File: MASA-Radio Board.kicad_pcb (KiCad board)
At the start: 4 copper layers, 75.8 x 76.2 mm, 70 parts, among them IC1 FAN4010IL6X_F113, IC2 FAN4010IL6X_F113, J1 Conn_01x02, J2 Conn_01x02_Male, J3 Conn_01x06, J4 Conn_01x03_Male, J5 SC_19-20, J6 Conn_01x06, J7 Conn_01x02, J8 UJ2-MBH-1-SMT-TR, U1 MP5077GG-Z, U2 BL654PA, U3 MIC5504-3.3YM5, U5 MP5077GG-Z, U6 SN74LVC1T45DBVR, U7 SN65HVD1050D, U8 MCP2515-xSO, U9 SN74LVC1T45DBVR

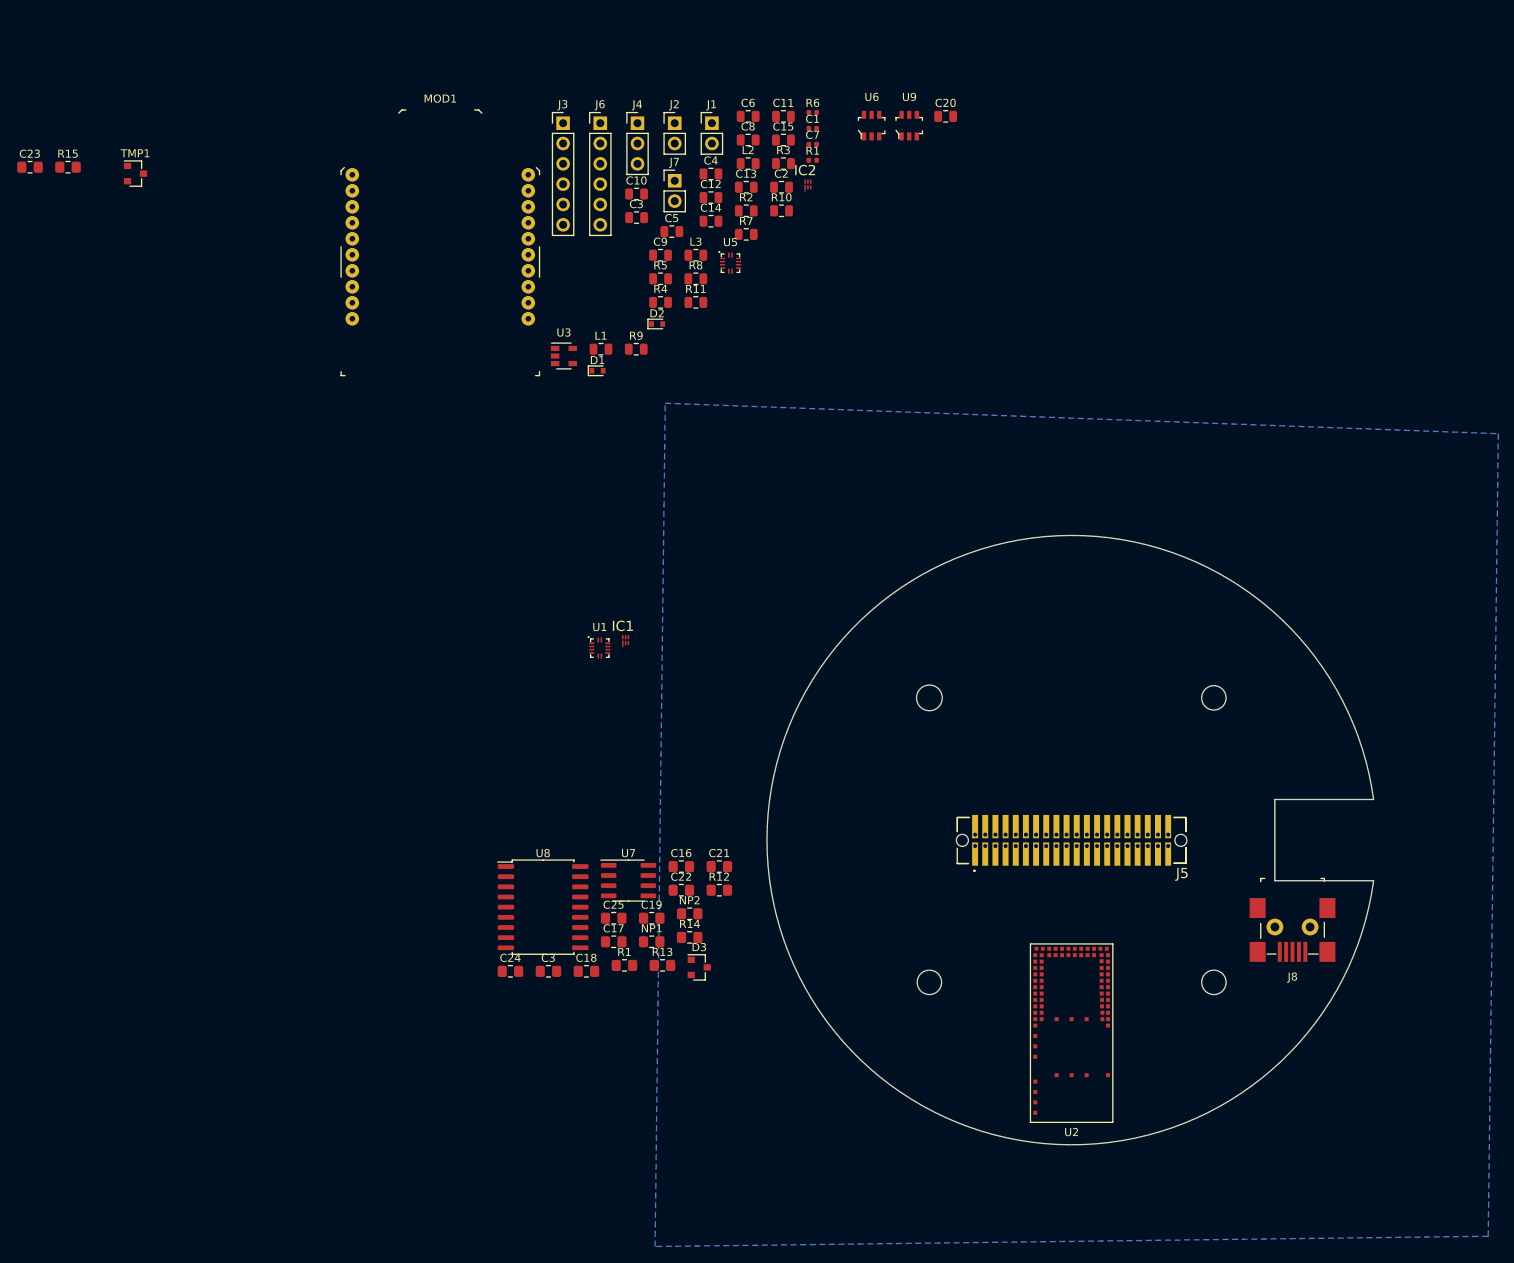
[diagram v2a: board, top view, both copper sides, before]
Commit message: added solder bridges, placed a few components on board
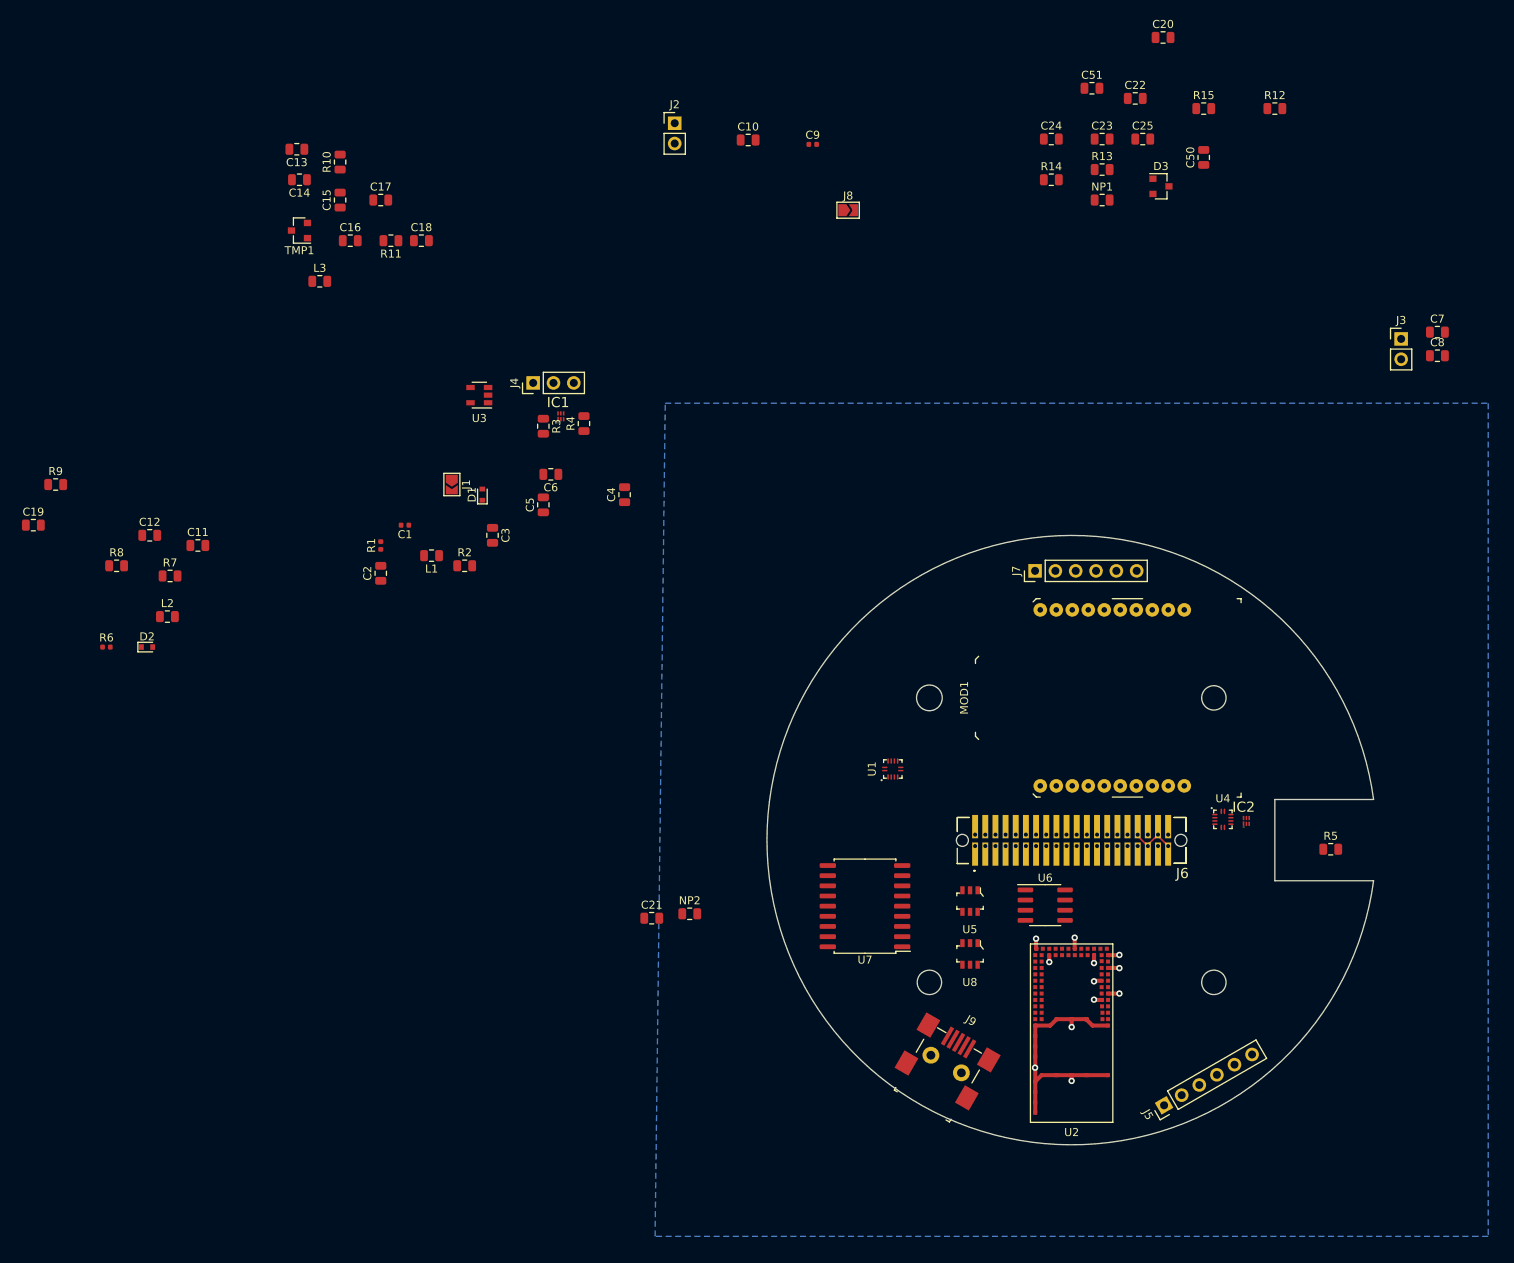
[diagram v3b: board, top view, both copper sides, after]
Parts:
- removed the C3 at (87.0, 143.4)
- removed the R1 at (96.5, 142.7)
- added C7: 47pF, Capacitor_SMD:C_0805_2012Metric, F.Cu at (198.1, 63.5)
- added C8: 1uF, Capacitor_SMD:C_0805_2012Metric, F.Cu at (198.1, 66.5)
- added J3: Conn_01x02_Male, Connector_PinHeader_2.54mm:PinHeader_1x02_P2.54mm_Vertical, F.Cu at (193.6, 64.3)
- C18: renamed from C16; footprint Capacitor_SMD:C_0805_2012Metric_Pad1.15x1.40mm_HandSolder -> Capacitor_SMD:C_0805_2012Metric
- C19: renamed from C17; footprint Capacitor_SMD:C_0805_2012Metric_Pad1.15x1.40mm_HandSolder -> Capacitor_SMD:C_0805_2012Metric
- C20: renamed from C18; footprint Capacitor_SMD:C_0805_2012Metric_Pad1.15x1.40mm_HandSolder -> Capacitor_SMD:C_0805_2012Metric
- C21: renamed from C19; footprint Capacitor_SMD:C_0805_2012Metric_Pad1.15x1.40mm_HandSolder -> Capacitor_SMD:C_0805_2012Metric
- C23: renamed from C21; footprint Capacitor_SMD:C_0805_2012Metric_Pad1.15x1.40mm_HandSolder -> Capacitor_SMD:C_0805_2012Metric
- C24: renamed from C22; footprint Capacitor_SMD:C_0805_2012Metric_Pad1.15x1.40mm_HandSolder -> Capacitor_SMD:C_0805_2012Metric
- C25: renamed from C23; footprint Capacitor_SMD:C_0805_2012Metric_Pad1.15x1.40mm_HandSolder -> Capacitor_SMD:C_0805_2012Metric
- C50: renamed from C24; footprint Capacitor_SMD:C_0805_2012Metric_Pad1.15x1.40mm_HandSolder -> Capacitor_SMD:C_0805_2012Metric
- C51: renamed from C25; footprint Capacitor_SMD:C_0805_2012Metric_Pad1.15x1.40mm_HandSolder -> Capacitor_SMD:C_0805_2012Metric
- J1: footprint Connector_PinHeader_2.54mm:PinHeader_1x02_P2.54mm_Vertical -> Jumper:SolderJumper-2_P1.3mm_Open_TrianglePad1.0x1.5mm
- J8: renamed from J7; footprint Connector_PinHeader_2.54mm:PinHeader_1x02_P2.54mm_Vertical -> Jumper:SolderJumper-2_P1.3mm_Open_TrianglePad1.0x1.5mm
- NP1, NP2, R12, R13, R14, R15: footprint Resistor_SMD:R_0805_2012Metric_Pad1.15x1.40mm_HandSolder -> Resistor_SMD:R_0805_2012Metric
- moved J5 143.9 mm to (164.0, 160.1), turned to 120 degrees
- moved R15 142.2 mm to (168.9, 35.6)
- moved C25 139.1 mm to (161.3, 39.4)
- moved C20 137.2 mm to (163.8, 26.7)
- moved C50 133.6 mm to (168.9, 41.7), turned to 90 degrees
- moved R12 119.9 mm to (177.8, 35.6)
- moved C51 119.7 mm to (154.9, 33.0)
- moved R13 113.7 mm to (156.2, 43.2)
- moved D3 113.4 mm to (163.6, 45.3)
- moved R6 110.7 mm to (31.8, 102.9)
- moved R5 110.0 mm to (184.8, 128.1)
- moved NP1 108.5 mm to (156.2, 47.0)
- moved R14 104.9 mm to (149.9, 44.5)
- moved C24 104.7 mm to (149.9, 39.4)
- moved U8 103.8 mm to (139.7, 141.2), turned to 180 degrees
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- renumbered C8 to C10, C9 to C11, C10 to C12, C11 to C13, C12 to C14, C13 to C15, C14 to C16, C15 to C17, C20 to C22, C5 to C4, C6 to C5, C4 to C6, C7 to C9, J3 to J5, J5 to J6, J6 to J7, J8 to J9, U5 to U4, U6 to U5, U7 to U6, U8 to U7, U9 to U8
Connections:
- J5 pad 2: UART_CTS -> UART_RTS
- J5 pad 6: UART_RTS -> UART_CTS
- U2 pad 1: Net-(U2-Pad1) -> SWDIO
- U2 pad 3: Net-(U2-Pad3) -> SWDCLK
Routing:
- net GND: track 0.00 -> 42.8 mm, vias 0 -> 12
- net 5V0: track 0.00 -> 5.87 mm
- added copper zone on In1.Cu, net +3V3
- added copper zone on B.Cu, net GND
- removed copper zone on B.Cu, net +3V3
- removed copper zone on In1.Cu, net GND
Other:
- rule trace_min: 0.2 -> 0.1524
- rule via_min_drill: 0.3 -> 0.254
- rule via_min_size: 0.4 -> 0.3048

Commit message: Moved components
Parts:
- removed J5: Conn_01x06, Connector_PinHeader_2.54mm:PinHeader_1x06_P2.54mm_Vertical
- moved J7 67.2 mm to (171.9, 156.1), turned to 135 degrees
- moved J9 60.4 mm to (180.6, 120.2), turned to 0 degrees
- moved U2 49.7 mm to (153.1, 101.5), turned to 0 degrees
- moved MOD1 41.6 mm to (151.8, 150.4)
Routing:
- net GND: track 42.8 -> 0.00 mm, vias 12 -> 0

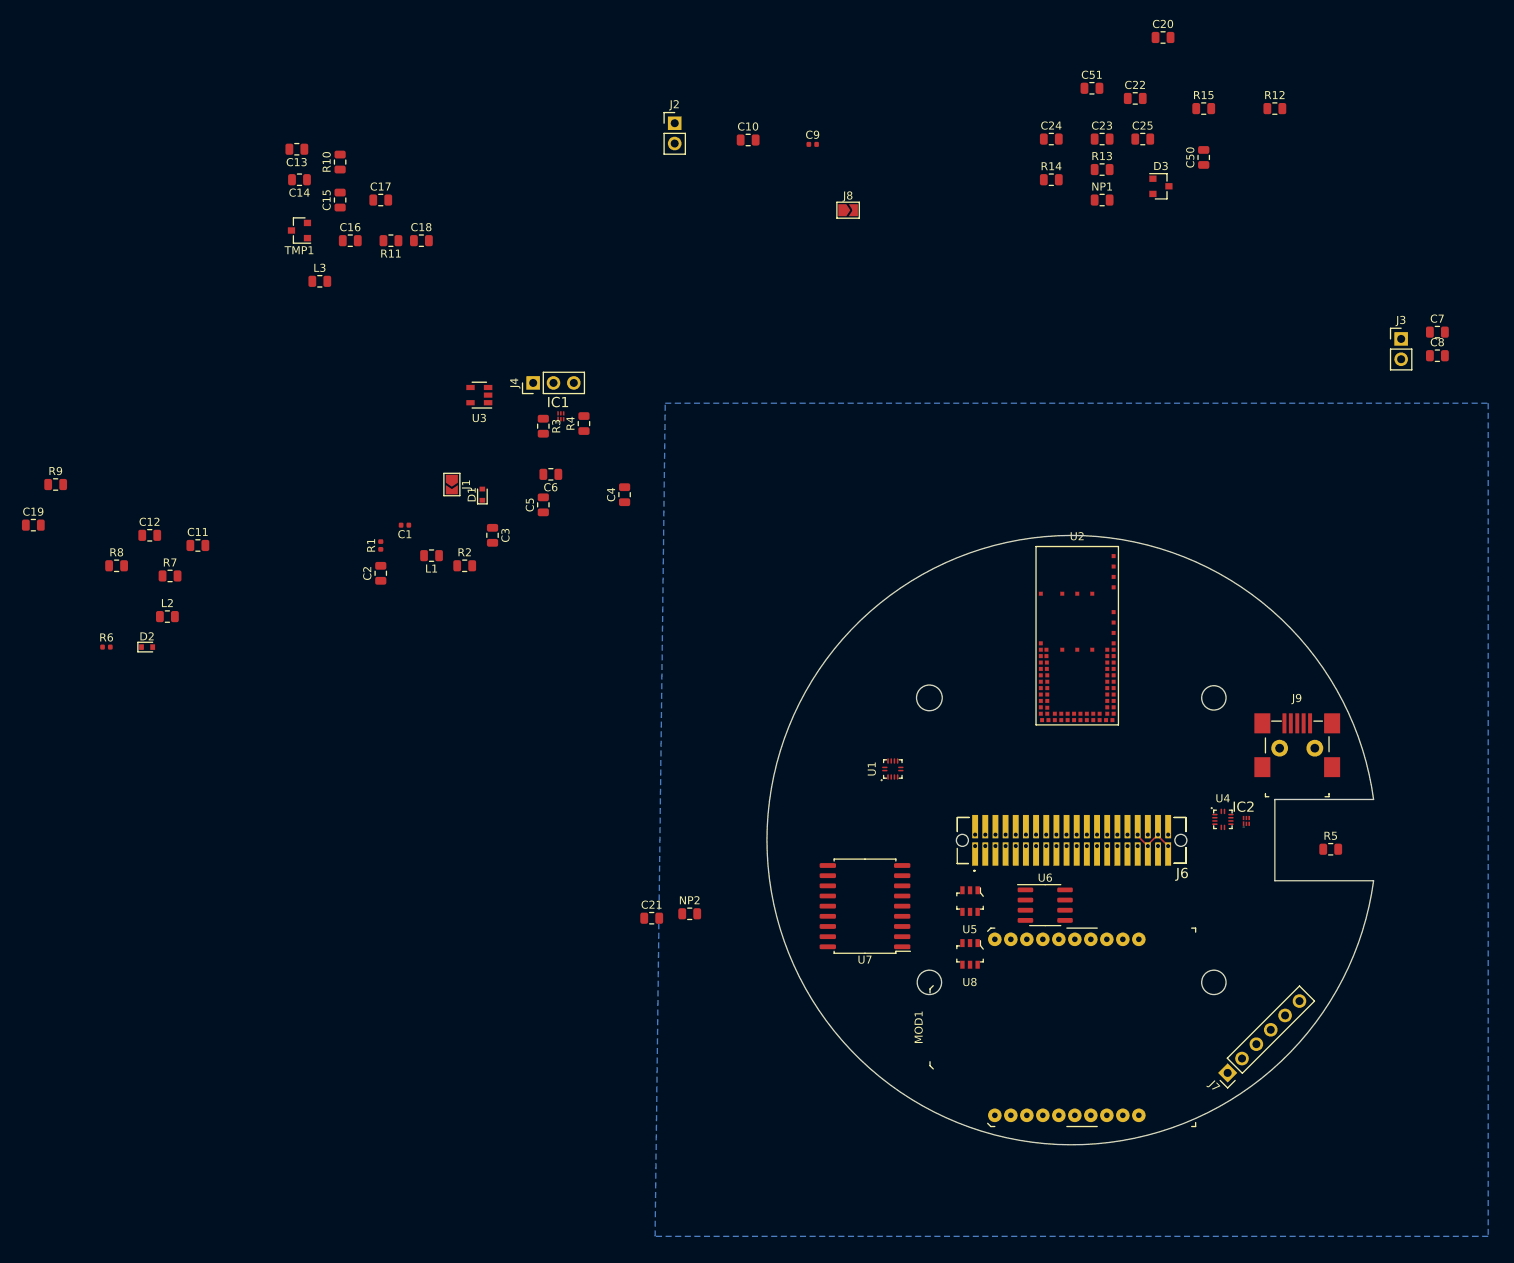
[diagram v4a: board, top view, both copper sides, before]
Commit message: A very rough placement of components, some routing
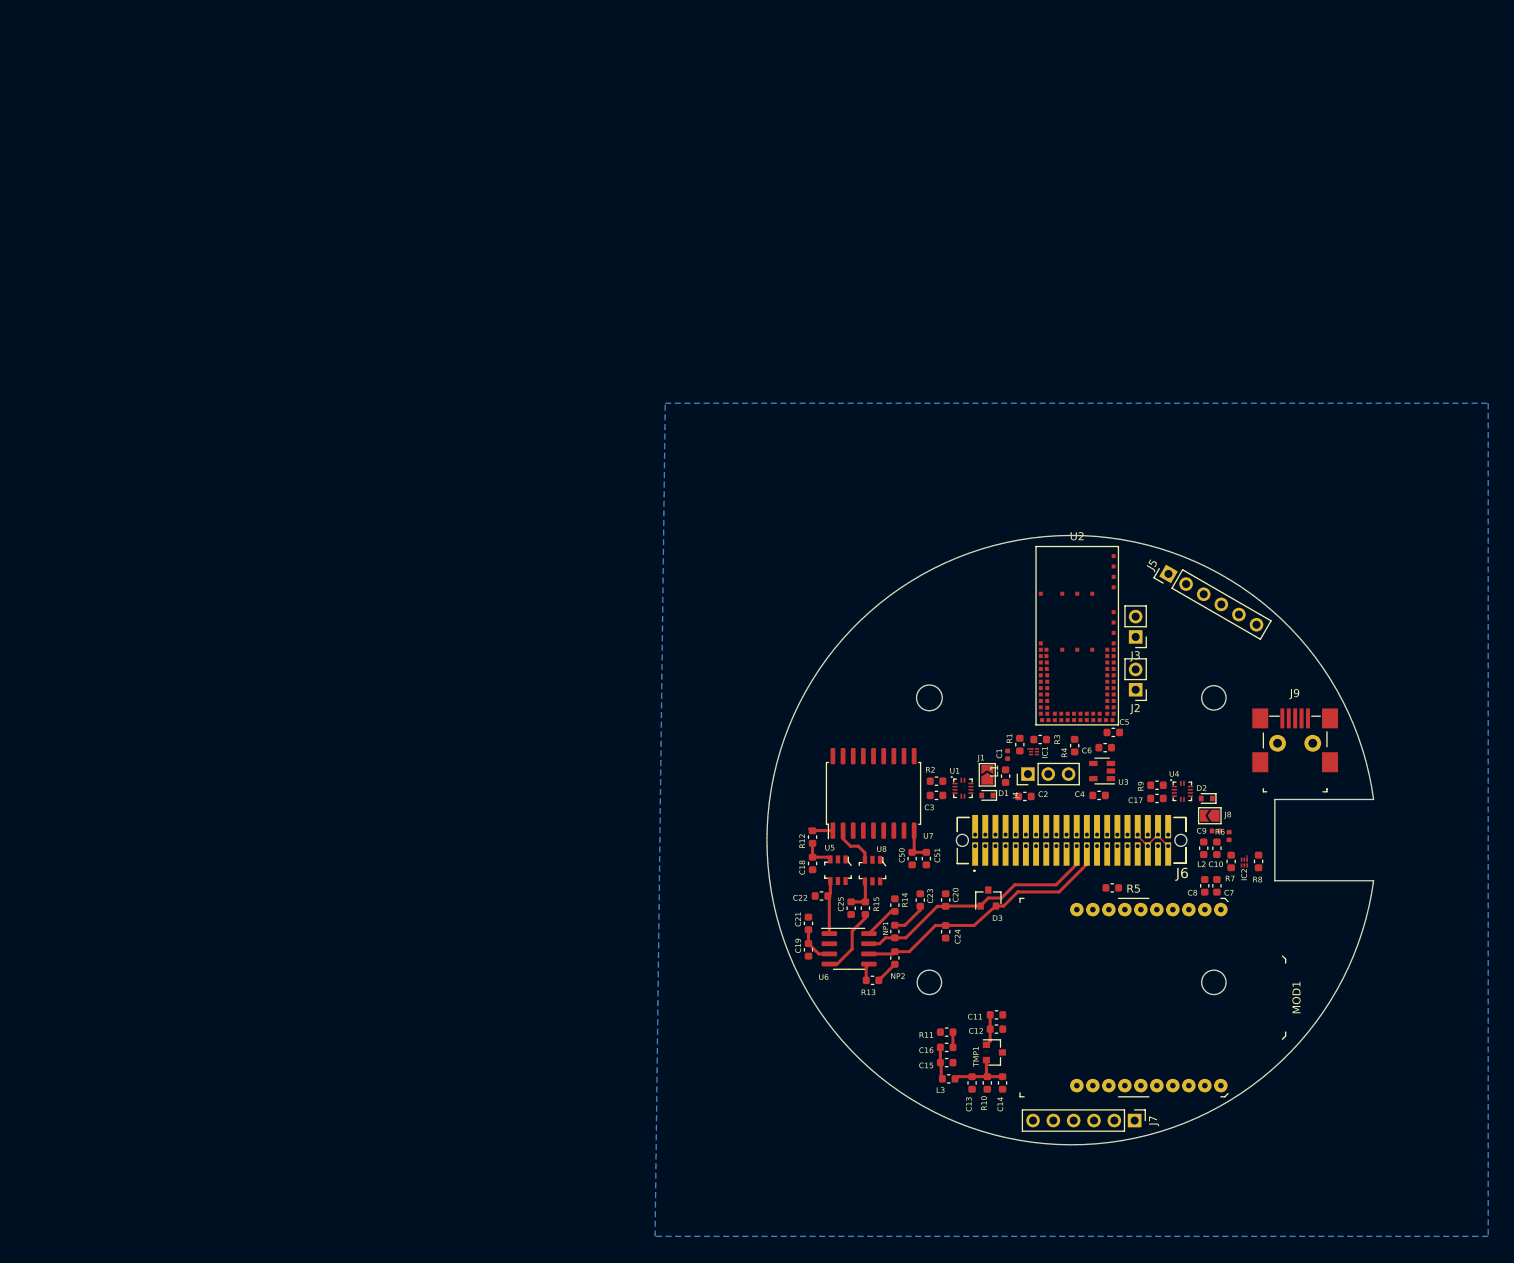
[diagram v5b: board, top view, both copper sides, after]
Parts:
- added J5: Conn_01x06, Connector_PinHeader_2.54mm:PinHeader_1x06_P2.54mm_Vertical, F.Cu at (164.5, 93.7)
- C10, C11, C12, C13, C14, C15, C16, C17, C18, C19, C2, C20, C21, C22, C23, C24, C25, C3, C4, C5, C50, C51, C6, C7, C8: footprint Capacitor_SMD:C_0805_2012Metric -> Capacitor_SMD:C_0603_1608Metric
- D3: value D5V0L2B3W-7 -> D_TVS_x2_AAC
- L1, L2, L3: footprint Inductor_SMD:L_0805_2012Metric -> Inductor_SMD:L_0603_1608Metric
- NP1, NP2, R10, R11, R12, R13, R14, R15, R2, R3, R4, R5, R7, R8, R9: footprint Resistor_SMD:R_0805_2012Metric -> Resistor_SMD:R_0603_1608Metric
- R1: footprint Resistor_SMD:R_0402_1005Metric -> Resistor_SMD:R_0603_1608Metric
- moved R8 147.5 mm to (175.8, 129.7), turned to 270 degrees
- moved C13 144.0 mm to (140.0, 157.4), turned to 270 degrees
- moved C14 143.1 mm to (143.8, 157.4), turned to 270 degrees
- moved R9 142.7 mm to (163.1, 120.1)
- moved R6 142.3 mm to (172.1, 126.5), turned to 270 degrees
- moved R10 140.7 mm to (141.9, 157.4), turned to 270 degrees
- moved R7 137.4 mm to (172.3, 129.7), turned to 270 degrees
- moved TMP1 134.5 mm to (142.7, 153.5), turned to 0 degrees
- moved D2 133.8 mm to (169.3, 121.8), turned to 180 degrees
- moved L2 132.7 mm to (168.9, 128.0), turned to 270 degrees
- moved C15 131.8 mm to (136.8, 154.8), turned to 0 degrees
- moved L3 127.0 mm to (137.0, 156.8), turned to 180 degrees
- moved C16 125.4 mm to (136.8, 152.9)
- moved C12 122.5 mm to (143.0, 150.6)
- moved C17 122.5 mm to (163.1, 121.8), turned to 180 degrees
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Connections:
- D3 pad 1: GND -> CAN_H
- D3 pad 2: CAN_H -> CAN_L
- D3 pad 3: CAN_L -> GND
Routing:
- net CAN_L: track 0.00 -> 34.1 mm
- net CAN_H: track 0.00 -> 32.6 mm
- net Net-(R15-Pad1): track 0.00 -> 9.07 mm
- net +5V: track 0.00 -> 8.81 mm
- net Net-(C13-Pad1): track 0.00 -> 8.03 mm
- net Net-(C23-Pad1): track 0.00 -> 7.25 mm
- net Net-(C22-Pad2): track 0.00 -> 6.87 mm
- net Net-(U7-Pad2): track 0.00 -> 5.36 mm
- net +3V3: track 0.00 -> 4.60 mm
- net Net-(C25-Pad1): track 0.00 -> 4.45 mm
- net Net-(R14-Pad1): track 0.00 -> 4.42 mm
- net Net-(C18-Pad1): track 0.00 -> 4.25 mm
- net TSENSE: track 0.00 -> 3.98 mm
- net Net-(R12-Pad2): track 0.00 -> 2.84 mm
- net Net-(R13-Pad1): track 0.00 -> 2.30 mm
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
